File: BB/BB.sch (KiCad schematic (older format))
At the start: 234 parts, among them SW0 SW_Push, U1 AT90USB1286-AU, Y0 16Mhz

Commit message: Rows Done
Main Columns
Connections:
- net COL0: now also U1.37 (PC2)
- net COL1: now also U1.38 (PC3)
- net COL10: now also U1.48 (PA3)
- net COL11: now also U1.49 (PA2)
- net COL12: now also U1.50 (PA1)
- net COL13: now also U1.51 (PA0)
- net COL14: now also U1.54 (PF7)
- net COL15: now also U1.55 (PF6)
- net COL16: now also U1.56 (PF5)
- net COL17: now also U1.57 (PF4)
- net COL18: now also U1.58 (PF3)
- net COL19: now also U1.59 (PF2)
- net COL2: now also U1.39 (PC4)
- net COL20: now also U1.60 (PF1)
- net COL21: now also U1.61 (PF0)
- net COL3: now also U1.40 (PC5)
- net COL4: now also U1.41 (PC6); no longer MX67.3 (LED)
- net COL5: now also U1.42 (PC7)
- net COL6: now also U1.44 (PA7)
- net COL7: now also U1.45 (PA6)
- net COL8: now also U1.46 (PA5)
- net COL9: now also U1.47 (PA4)
- net ROW0: now also U1.25 (PD0)
- net ROW1: now also U1.26 (PD1)
- net ROW2: now also U1.27 (PD2)
- net ROW3: now also U1.28 (PD3)
- net ROW4: now also U1.29 (PD4)
- net ROW5: now also U1.30 (PD5)
- net ROW6: now also U1.31 (PD6)
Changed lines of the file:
@@
-$EndComp
-$Comp
-L MX_Alps_Hybrids:MX-1.75U MX67
-U 1 1 5CCE5F08
-P 8445 5655
-F 0 "MX67" H 8531 5872 60  0000 C CNN
-F 1 "MX-1.75U" H 8531 5798 20  0000 C CNN
-F 2 "MX_Alps_Hybrid:MX-1.75U" H 8420 5630 60  0001 C CNN
-F 3 "" H 8420 5630 60  0001 C CNN
-	1    8445 5655
-	1    0    0    -1
 $EndComp
 $Comp
@@
 COL3
 Wire Wire Line
-	8570 4285 8570 5680
-Wire Wire Line
 	8570 7010 8540 7010
-Connection ~ 8570 5680
-Wire Wire Line
-	8570 5680 8570 7010
 Wire Wire Line
 	8570 4285 8570 3600
-Connection ~ 8570 4285
 Wire Wire Line
 	8570 3600 8570 3155
@@
 Wire Wire Line
 	8620 4980 8615 4980
-Connection ~ 8620 5630
 Wire Wire Line
 	8620 4980 8620 4725
@@
 	1    0    0    -1
 $EndComp
+Text GLabel 4785 4410 2    50   Input ~ 0
+COL0
+Text GLabel 4785 4510 2    50   Input ~ 0
+COL1
+Text GLabel 4785 4610 2    50   Input ~ 0
+COL2
+Text GLabel 4785 4710 2    50   Input ~ 0
+COL3
+Text GLabel 4785 4810 2    50   Input ~ 0
+COL4
+Text GLabel 4785 4910 2    50   Input ~ 0
+COL5
+Text GLabel 4785 3110 2    50   Input ~ 0
+COL6
+Text GLabel 4785 3010 2    50   Input ~ 0
+COL7
+Text GLabel 4785 2910 2    50   Input ~ 0
+COL8
+Text GLabel 4785 2810 2    50   Input ~ 0
+COL9
+Text GLabel 4785 2710 2    50   Input ~ 0
+COL10
+Text GLabel 4785 2610 2    50   Input ~ 0
+COL11
+Text GLabel 4785 2510 2    50   Input ~ 0
+COL12
+Text GLabel 4785 2410 2    50   Input ~ 0
+COL13
+Text GLabel 3585 5810 0    50   Input ~ 0
+COL14
+Text GLabel 3585 5710 0    50   Input ~ 0
+COL15
+Text GLabel 3585 5610 0    50   Input ~ 0
+COL16
+Text GLabel 3585 5510 0    50   Input ~ 0
+COL17
+Text GLabel 3585 5410 0    50   Input ~ 0
+COL18
+Text GLabel 3585 5310 0    50   Input ~ 0
+COL19
+Text GLabel 3585 5210 0    50   Input ~ 0
+COL20
+Text GLabel 3585 5110 0    50   Input ~ 0
+COL21
+Text GLabel 4785 5110 2    50   Input ~ 0
+ROW0
+Text GLabel 4785 5210 2    50   Input ~ 0
+ROW1
+Text GLabel 4785 5310 2    50   Input ~ 0
+ROW2
+Text GLabel 4785 5410 2    50   Input ~ 0
+ROW3
+Text GLabel 4785 5510 2    50   Input ~ 0
+ROW4
+Text GLabel 4785 5610 2    50   Input ~ 0
+ROW5
+Text GLabel 4785 5710 2    50   Input ~ 0
+ROW6
+Connection ~ 8620 5630
+$Comp
+L MX_Alps_Hybrids:MX-1.75U MX67
+U 1 1 5CCE5F08
+P 8445 5655
+F 0 "MX67" H 8531 5872 60  0000 C CNN
+F 1 "MX-1.75U" H 8531 5798 20  0000 C CNN
+F 2 "MX_Alps_Hybrid:MX-1.75U" H 8420 5630 60  0001 C CNN
+F 3 "" H 8420 5630 60  0001 C CNN
+	1    8445 5655
+	1    0    0    -1
+$EndComp
+Wire Wire Line
+	8570 7010 8570 5735
+Wire Wire Line
+	8570 5735 8695 5735
+Wire Wire Line
+	8695 5735 8695 5540
+Wire Wire Line
+	8695 5540 8570 5540
+Wire Wire Line
+	8570 5540 8570 4285
+Connection ~ 8570 4285
 $EndSCHEMATC

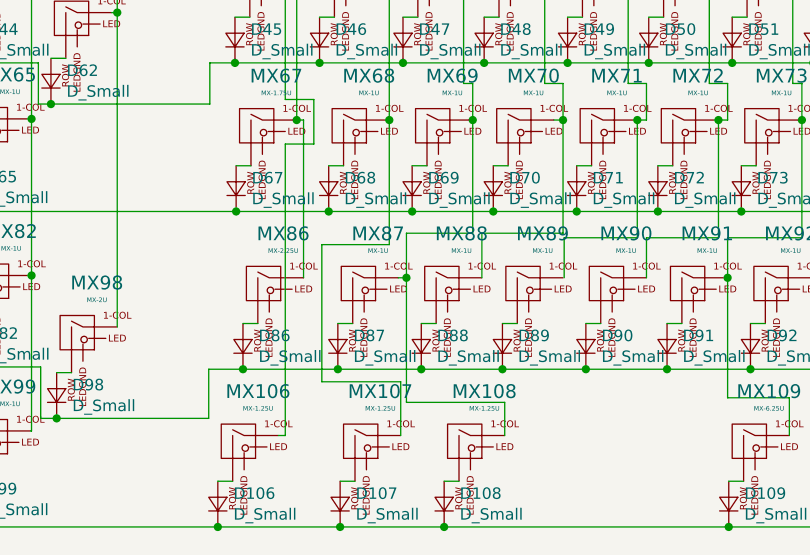
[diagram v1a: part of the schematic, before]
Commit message: MCU Wired
No rows or colomns
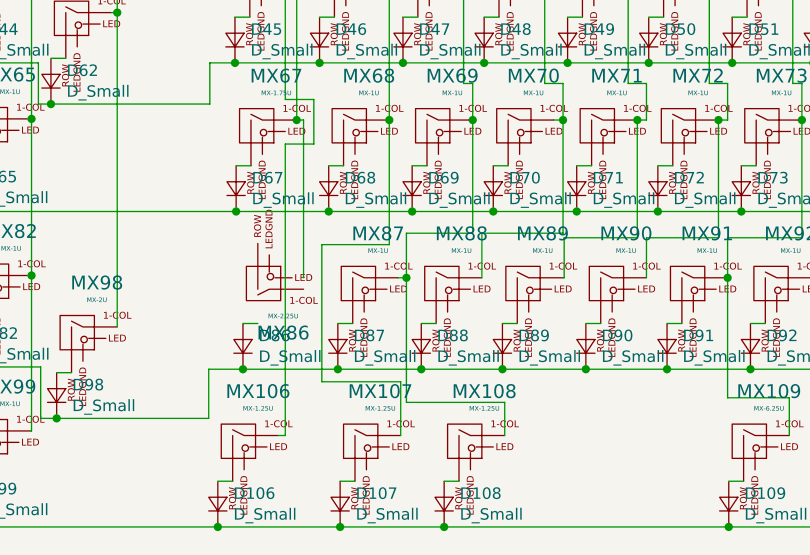
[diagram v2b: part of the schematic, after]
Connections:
- net COL5: no longer MX86.1 (COL)
- net COL9: now also MX89.1 (COL)
- net at MX86.2 (ROW): no longer D86.2 (A)
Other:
- moved on the sheet: MX86
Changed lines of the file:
@@
 F 3 "" H 8450 6320 60  0001 C CNN
 	1    8475 6345
-	1    0    0    -1
+	1    0    0    1
 $EndComp
 $Comp
@@
 	8570 5540 8570 4285
 Connection ~ 8570 4285
+Wire Wire Line
+	9790 6320 9785 6320
 $EndSCHEMATC
